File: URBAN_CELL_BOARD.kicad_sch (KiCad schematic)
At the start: 15 parts, among them J1 Conn_02x09_Odd_Even, J2 Conn_01x02_Female, J3 Conn_01x02_Female

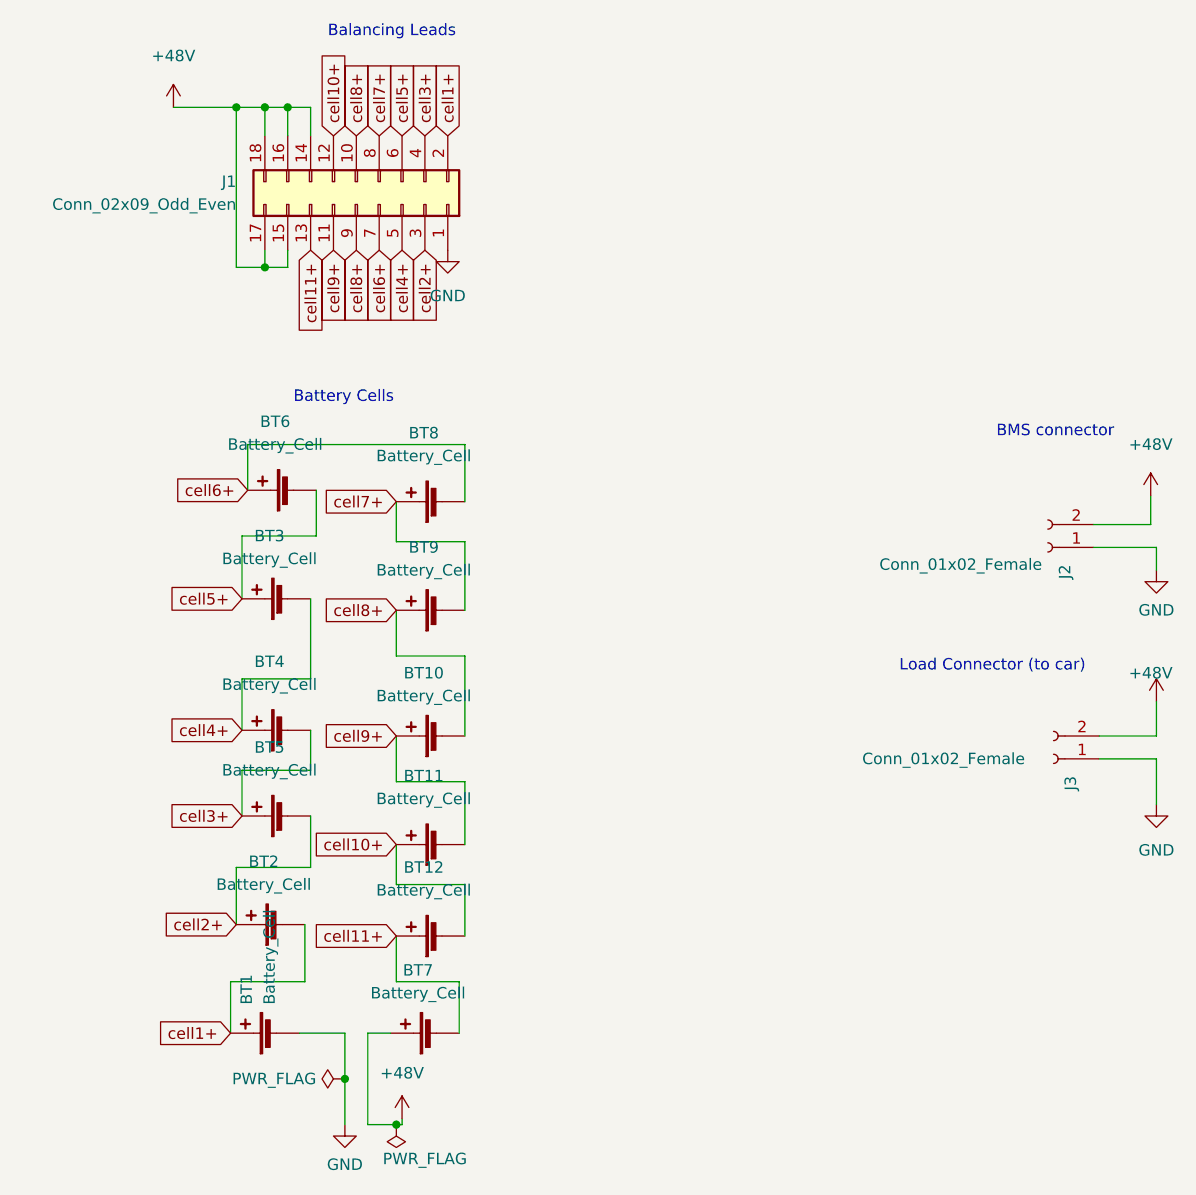
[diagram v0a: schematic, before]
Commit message: most of layout done and custom footprints made for battery blocks
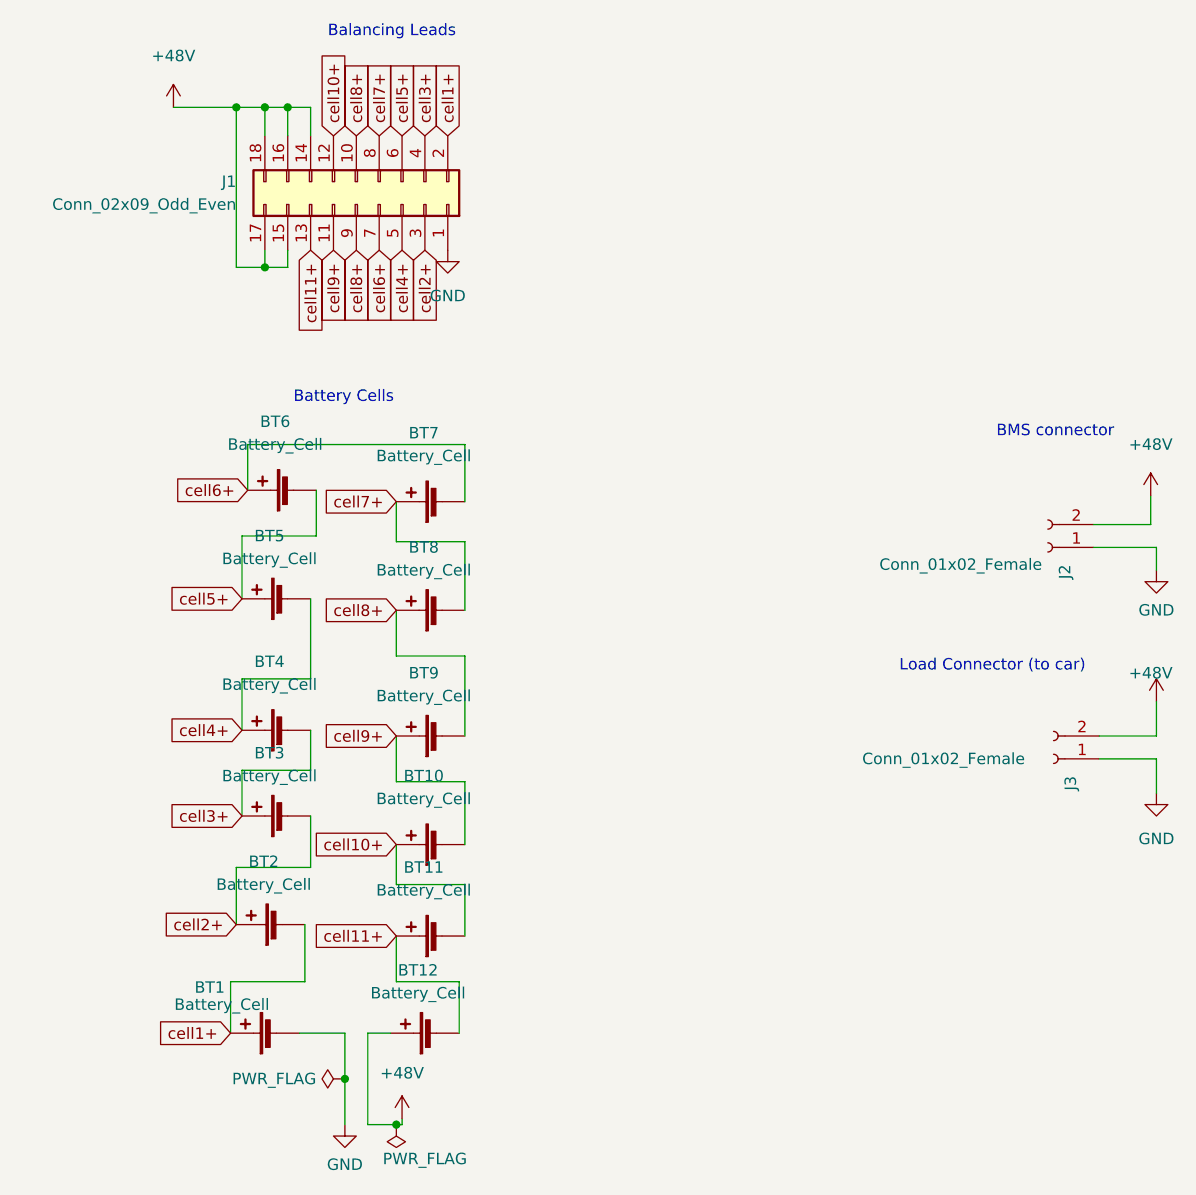
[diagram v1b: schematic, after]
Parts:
- BT1, BT2, BT4, BT6: footprint (none) -> Battery:Energus Li1x4pVTC6T
- BT10: renamed from BT11; footprint (none) -> Battery:Energus Li1x4pVTC6T
- BT11: renamed from BT12; footprint (none) -> Battery:Energus Li1x4pVTC6T
- BT12: renamed from BT7; footprint (none) -> Battery:Energus Li1x4pVTC6T
- BT3: renamed from BT5; footprint (none) -> Battery:Energus Li1x4pVTC6T
- BT5: renamed from BT3; footprint (none) -> Battery:Energus Li1x4pVTC6T
- BT7: renamed from BT8; footprint (none) -> Battery:Energus Li1x4pVTC6T
- BT8: renamed from BT9; footprint (none) -> Battery:Energus Li1x4pVTC6T
- BT9: renamed from BT10; footprint (none) -> Battery:Energus Li1x4pVTC6T
- J3: footprint TerminalBlock_TE-Connectivity:TE_1986660-2 -> TerminalBlock_TE-Connectivity:TerminalBlock_TE_282834-2_1x02_P2.54mm_Horizontal

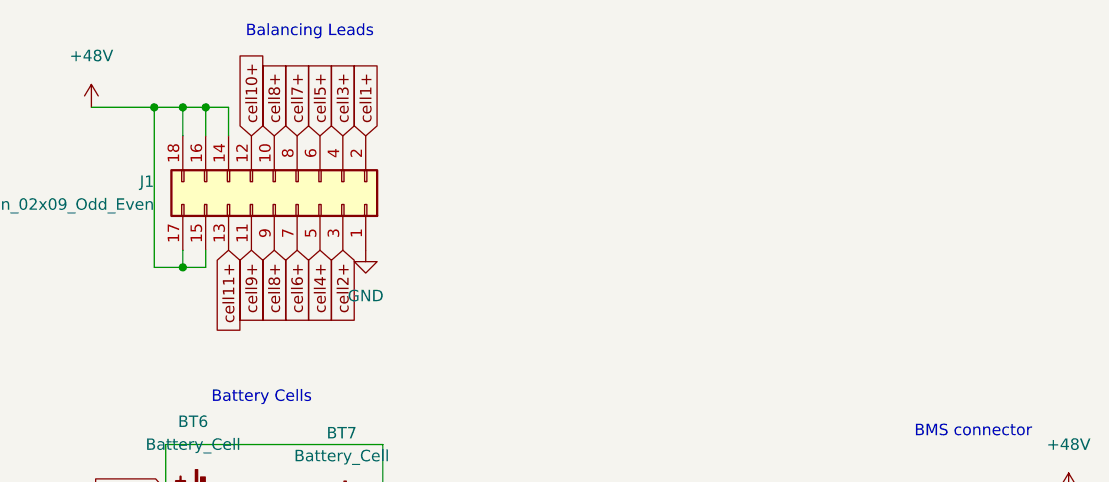
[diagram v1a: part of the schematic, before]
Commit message: fixed connector footprints, edited connector symbols, added mounting holes, solved DRC routing issue, created 48V and GND filled zones around one connector, made silkscreen edits
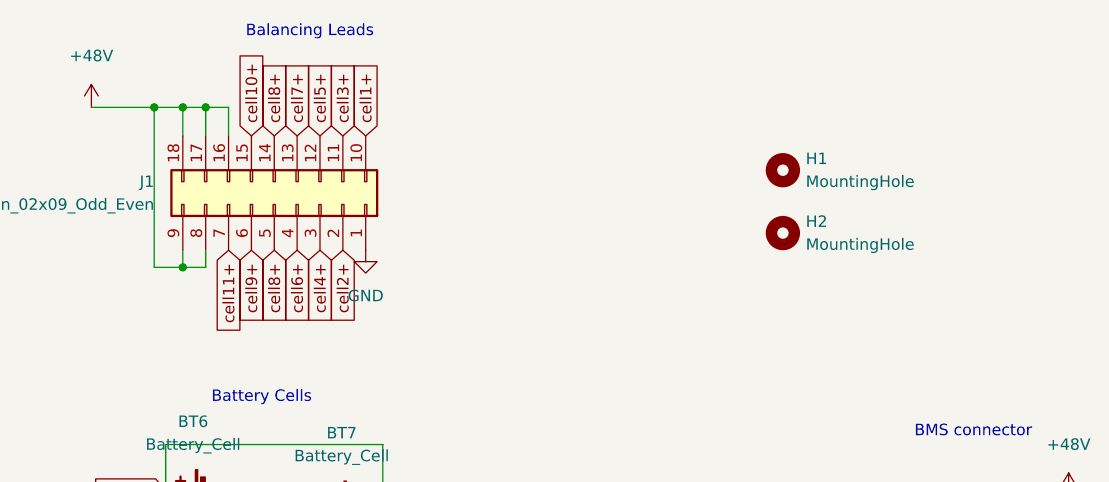
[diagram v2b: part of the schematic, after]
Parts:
- added H1, H2: MountingHole, MountingHole:MountingHole_8.4mm_M8, symbol Mechanical:MountingHole
- J1: symbol Connector_Generic:Conn_02x09_Odd_Even -> Connector_Generic:Conn_02x09_Top_Bottom
- J3: footprint TerminalBlock_TE-Connectivity:TerminalBlock_TE_282834-2_1x02_P2.54mm_Horizontal -> TerminalBlock_TE-Connectivity:TE_1986660-2
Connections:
- net +48V: now also J1.8 (Pin_8), J1.9 (Pin_9); no longer J1.14 (Pin_14), J1.15 (Pin_15)
- net cell1+: now also J1.10 (Pin_10); no longer J1.2 (Pin_2)
- net cell10+: now also J1.15 (Pin_15); no longer J1.12 (Pin_12)
- net cell11+: now also J1.7 (Pin_7); no longer J1.13 (Pin_13)
- net cell2+: now also J1.2 (Pin_2); no longer J1.3 (Pin_3)
- net cell3+: now also J1.11 (Pin_11); no longer J1.4 (Pin_4)
- net cell4+: now also J1.3 (Pin_3); no longer J1.5 (Pin_5)
- net cell5+: now also J1.12 (Pin_12); no longer J1.6 (Pin_6)
- net cell6+: now also J1.4 (Pin_4); no longer J1.7 (Pin_7)
- net cell7+: now also J1.13 (Pin_13); no longer J1.8 (Pin_8)
- net cell8+: now also J1.14 (Pin_14), J1.5 (Pin_5); no longer J1.10 (Pin_10), J1.9 (Pin_9)
- net cell9+: now also J1.6 (Pin_6); no longer J1.11 (Pin_11)
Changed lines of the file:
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@@
     (pin "2")
   )
-  (symbol (lib_id "Connector_Generic:Conn_02x09_Odd_Even") (at 59.055 33.02 270) (mirror x) (unit 1)
+  (symbol (lib_id "Mechanical:MountingHole") (at 115.57 29.21 0) (unit 1)
+    (in_bom yes) (on_board yes) (fields_autoplaced)
+    (property "Reference" "H1" (id 0) (at 118.11 27.9399 0)
+      (effects (font (size 1.27 1.27)) (justify left))
+    )
+    (property "Value" "MountingHole" (id 1) (at 118.11 30.4799 0)
+      (effects (font (size 1.27 1.27)) (justify left))
+    )
+    (property "Footprint" "MountingHole:MountingHole_8.4mm_M8" (id 2) (at 115.57 29.21 0)
+      (effects (font (size 1.27 1.27)) hide)
+    )
+    (property "Datasheet" "~" (id 3) (at 115.57 29.21 0)
+      (effects (font (size 1.27 1.27)) hide)
+    )
+  )
+  (symbol (lib_id "Connector_Generic:Conn_02x09_Top_Bottom") (at 59.055 33.02 270) (mirror x) (unit 1)
     (in_bom yes) (on_board yes) (fields_autoplaced)
     (property "Reference" "J1" (id 0) (at 45.72 30.4799 90)
@@
       (effects (font (size 1.27 1.27)) hide)
     )
-    (property "Datasheet" "https://www.digikey.ca/en/products/detail/molex/0039301182/930340" (id 3) (at 59.055 33.02 0)
+    (property "Datasheet" "~" (id 3) (at 59.055 33.02 0)
       (effects (font (size 1.27 1.27)) hide)
     )
@@
     (pin "1")
   )
+  (symbol (lib_id "Mechanical:MountingHole") (at 115.57 36.195 0) (unit 1)
+    (in_bom yes) (on_board yes) (fields_autoplaced)
+    (property "Reference" "H2" (id 0) (at 118.11 34.9249 0)
+      (effects (font (size 1.27 1.27)) (justify left))
+    )
+    (property "Value" "MountingHole" (id 1) (at 118.11 37.4649 0)
+      (effects (font (size 1.27 1.27)) (justify left))
+    )
+    (property "Footprint" "MountingHole:MountingHole_8.4mm_M8" (id 2) (at 115.57 36.195 0)
+      (effects (font (size 1.27 1.27)) hide)
+    )
+    (property "Datasheet" "~" (id 3) (at 115.57 36.195 0)
+      (effects (font (size 1.27 1.27)) hide)
+    )
+  )
   (symbol (lib_id "power:PWR_FLAG") (at 57.785 130.175 90) (unit 1)
     (in_bom yes) (on_board yes) (fields_autoplaced)
@@
       (effects (font (size 1.27 1.27)) (justify left))
     )
-    (property "Footprint" "TerminalBlock_TE-Connectivity:TerminalBlock_TE_282834-2_1x02_P2.54mm_Horizontal" (id 2) (at 136.525 94.615 0)
+    (property "Footprint" "TerminalBlock_TE-Connectivity:TE_1986660-2" (id 2) (at 136.525 94.615 0)
       (effects (font (size 1.27 1.27)) hide)
     )
@@
       (reference "BT12") (unit 1) (value "Battery_Cell") (footprint "Battery:Energus Li1x4pVTC6T")
     )
+    (path "/7a60d2ea-6711-47ba-a176-51bc40723dbe"
+      (reference "H1") (unit 1) (value "MountingHole") (footprint "MountingHole:MountingHole_8.4mm_M8")
+    )
+    (path "/d0edf088-bf65-42bc-9ffa-7aea9ff5522c"
+      (reference "H2") (unit 1) (value "MountingHole") (footprint "MountingHole:MountingHole_8.4mm_M8")
+    )
     (path "/7dd28c58-6b6d-4976-852a-2e65cdece38e"
       (reference "J1") (unit 1) (value "Conn_02x09_Odd_Even") (footprint "Connector_Molex:Molex_Mini-Fit_Jr_5569-18A2_2x09_P4.20mm_Horizontal")
@@
     )
     (path "/d8409391-3828-4519-a15f-11b886edf7c0"
-      (reference "J3") (unit 1) (value "Conn_01x02_Female") (footprint "TerminalBlock_TE-Connectivity:TerminalBlock_TE_282834-2_1x02_P2.54mm_Horizontal")
-    )
-  )
+      (reference "J3") (unit 1) (value "Conn_01x02_Female") (footprint "TerminalBlock_TE-Connectivity:TE_1986660-2")
+    )
+  )

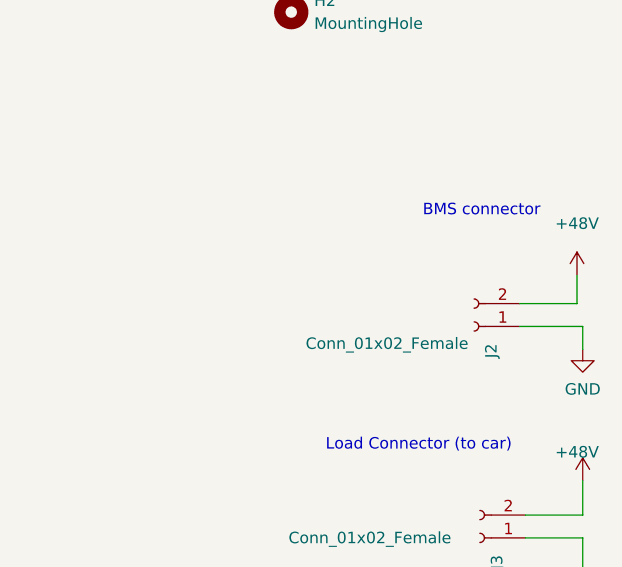
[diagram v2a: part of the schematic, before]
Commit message: replaced charge terminal with two larger single position ones, fixed labelling
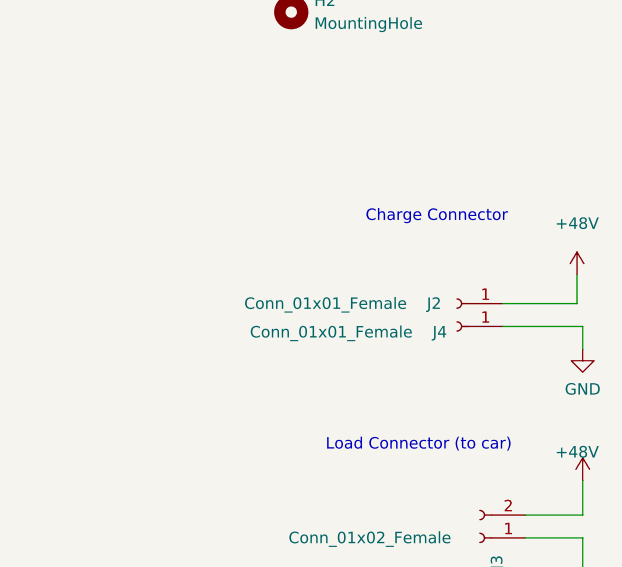
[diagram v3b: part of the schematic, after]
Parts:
- removed J2: Conn_01x02_Female, TerminalBlock_TE-Connectivity:TerminalBlock_TE_282834-2_1x02_P2.54mm_Horizontal, symbol Connector:Conn_01x02_Female
- added J2, J4: Conn_01x01_Female, Phoenix_1889262:1889262, symbol Connector:Conn_01x01_Female
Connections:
- net +48V: now also J2.1 (Pin_1)
- net GND: now also J4.1 (Pin_1)
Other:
- note added: "Charge Connector"
- note removed: "BMS connector"
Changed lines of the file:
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@@
     (stroke (width 0) (type default) (color 0 0 0 0))
   )
-  (wire (pts (xy 140.97 71.12) (xy 147.955 71.12))
+  (wire (pts (xy 139.065 71.12) (xy 147.955 71.12))
     (stroke (width 0) (type default) (color 0 0 0 0))
   )
@@
     (stroke (width 0) (type default) (color 0 0 0 0))
   )
-  (wire (pts (xy 140.97 68.58) (xy 147.32 68.58))
+  (wire (pts (xy 139.065 68.58) (xy 147.32 68.58))
     (stroke (width 0) (type default) (color 0 0 0 0))
   )
@@
     (effects (font (size 1.27 1.27)) (justify left bottom))
   )
-  (text "BMS connector\n" (at 130.175 59.055 0)
+  (text "Charge Connector" (at 123.825 59.69 0)
     (effects (font (size 1.27 1.27)) (justify left bottom))
   )
@@
     (pin "1")
   )
+  (symbol (lib_id "Connector:Conn_01x01_Female") (at 133.985 68.58 180) (unit 1)
+    (in_bom yes) (on_board yes)
+    (property "Reference" "J2" (id 0) (at 131.445 68.58 0))
+    (property "Value" "Conn_01x01_Female" (id 1) (at 119.38 68.58 0))
+    (property "Footprint" "Phoenix_1889262:1889262" (id 2) (at 133.985 68.58 0)
+      (effects (font (size 1.27 1.27)) hide)
+    )
+    (property "Datasheet" "https://media.digikey.com/pdf/Data%20Sheets/Phoenix%20Contact%20PDFs/1889262.pdf" (id 3) (at 133.985 68.58 0)
+      (effects (font (size 1.27 1.27)) hide)
+    )
+    (pin "1")
+  )
   (symbol (lib_id "Device:Battery_Cell") (at 68.58 92.075 90) (unit 1)
     (in_bom yes) (on_board yes) (fields_autoplaced)
@@
       (effects (font (size 1.27 1.27)) hide)
     )
+  )
+  (symbol (lib_id "Connector:Conn_01x01_Female") (at 133.985 71.12 180) (unit 1)
+    (in_bom yes) (on_board yes)
+    (property "Reference" "J4" (id 0) (at 132.08 71.755 0))
+    (property "Value" "Conn_01x01_Female" (id 1) (at 120.015 71.755 0))
+    (property "Footprint" "Phoenix_1889262:1889262" (id 2) (at 133.985 71.12 0)
+      (effects (font (size 1.27 1.27)) hide)
+    )
+    (property "Datasheet" "https://media.digikey.com/pdf/Data%20Sheets/Phoenix%20Contact%20PDFs/1889262.pdf" (id 3) (at 133.985 71.12 0)
+      (effects (font (size 1.27 1.27)) hide)
+    )
+    (pin "1")
   )
   (symbol (lib_id "Connector_Generic:Conn_02x09_Top_Bottom") (at 59.055 33.02 270) (mirror x) (unit 1)
@@
     (pin "9")
   )
-  (symbol (lib_id "Connector:Conn_01x02_Female") (at 135.89 71.12 180) (unit 1)
-    (in_bom yes) (on_board yes)
-    (property "Reference" "J2" (id 0) (at 137.7951 73.025 90)
-      (effects (font (size 1.27 1.27)) (justify left))
-    )
-    (property "Value" "Conn_01x02_Female" (id 1) (at 135.2551 73.025 0)
-      (effects (font (size 1.27 1.27)) (justify left))
-    )
-    (property "Footprint" "TerminalBlock_TE-Connectivity:TerminalBlock_TE_282834-2_1x02_P2.54mm_Horizontal" (id 2) (at 135.89 71.12 0)
-      (effects (font (size 1.27 1.27)) hide)
-    )
-    (property "Datasheet" "https://www.te.com/commerce/DocumentDelivery/DDEController?Action=srchrtrv&DocNm=282834&DocType=Customer+Drawing&DocLang=English" (id 3) (at 135.89 71.12 0)
-      (effects (font (size 1.27 1.27)) hide)
-    )
-    (pin "1")
-    (pin "2")
-  )
   (symbol (lib_id "Device:Battery_Cell") (at 68.58 114.3 90) (unit 1)
     (in_bom yes) (on_board yes) (fields_autoplaced)
@@
       (reference "J1") (unit 1) (value "Conn_02x09_Odd_Even") (footprint "Connector_Molex:Molex_Mini-Fit_Jr_5569-18A2_2x09_P4.20mm_Horizontal")
     )
-    (path "/83f74789-fc1c-4851-9e55-0808e022bb95"
-      (reference "J2") (unit 1) (value "Conn_01x02_Female") (footprint "TerminalBlock_TE-Connectivity:TerminalBlock_TE_282834-2_1x02_P2.54mm_Horizontal")
+    (path "/73835217-2342-4e74-b243-2594edd1a62e"
+      (reference "J2") (unit 1) (value "Conn_01x01_Female") (footprint "Phoenix_1889262:1889262")
     )
     (path "/d8409391-3828-4519-a15f-11b886edf7c0"
       (reference "J3") (unit 1) (value "Conn_01x02_Female") (footprint "TerminalBlock_TE-Connectivity:TE_1986660-2")
     )
-  )
+    (path "/7cd7a55c-d470-4b7c-ae21-15f755e6fe2d"
+      (reference "J4") (unit 1) (value "Conn_01x01_Female") (footprint "Phoenix_1889262:1889262")
+    )
+  )
